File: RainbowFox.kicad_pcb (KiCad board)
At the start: 2 copper layers, 304.8 x 95.3 mm, 316 parts, among them P1 FLASH_HDR, P2 CONN_01X06, P3 USB_OTG, P4 CONN_01X04, P5 CONN_01X02, P6 CONN_01X04, U1 MK20DX256VLH7, U2 IS31FL3737, U3 IS31FL3737, X1 CRYSTAL_SMD

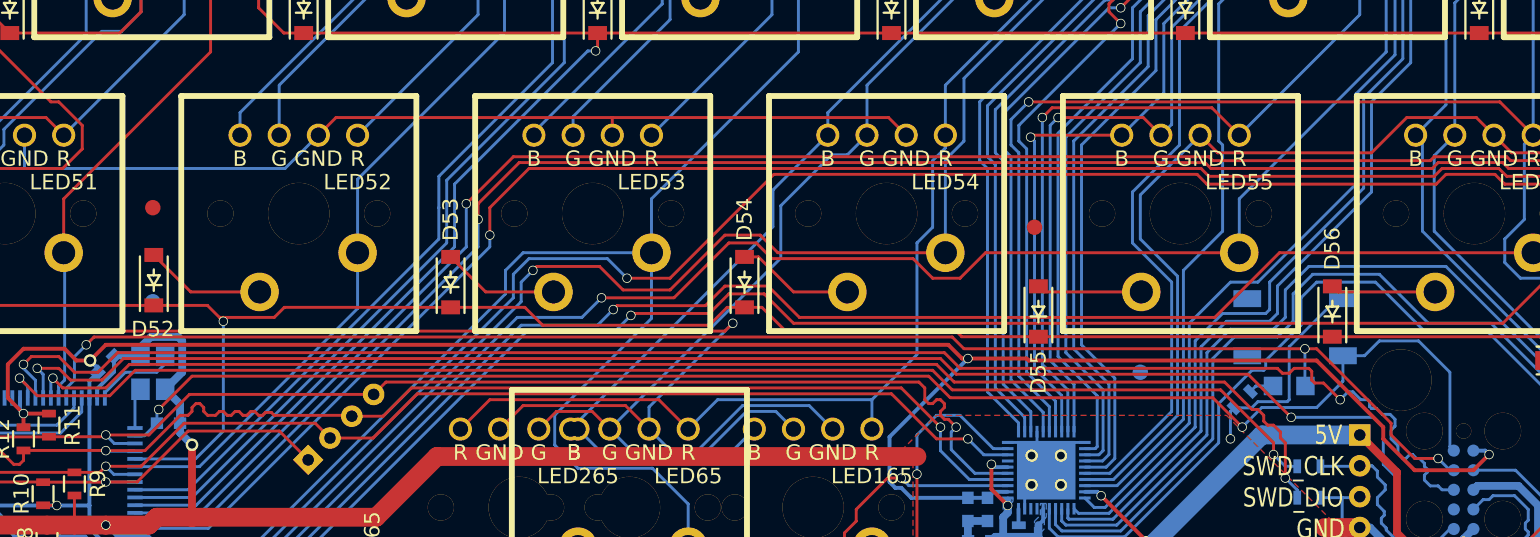
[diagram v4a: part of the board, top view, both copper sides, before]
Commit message: Properly replaced the Footprint of the Reset Switch
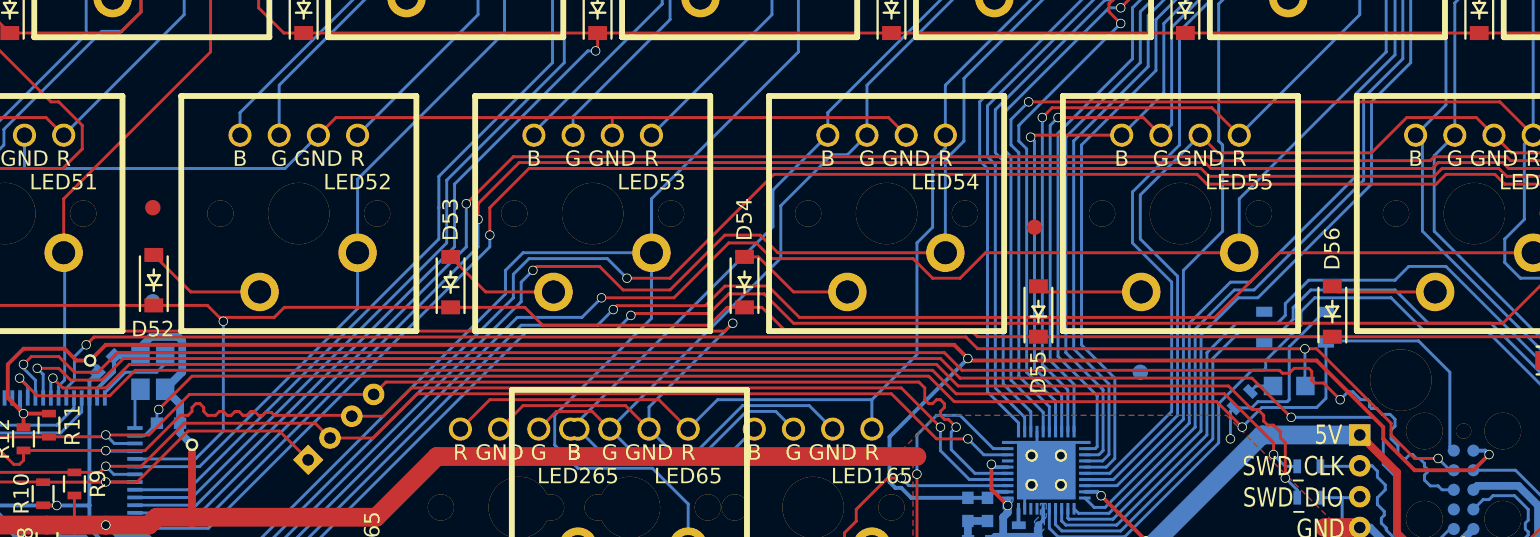
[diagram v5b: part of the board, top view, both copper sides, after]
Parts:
- S72: footprint lib.pretty:TACT_5.2x5.2 -> lib.pretty:PTS810
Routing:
- net GND: track 348.6 -> 346.4 mm
- net /ledmatrix/LED-B/CS9: track 176.0 -> 174.6 mm
- net /ledmatrix/LED-B/CS10: track 232.5 -> 231.2 mm
- net /mcu/MCU_RESET: track 98.0 -> 99.2 mm
- net /ledmatrix/LED-B/CS6: track 208.5 -> 207.6 mm
- net /ledmatrix/LED-B/CS7: track 241.7 -> 240.8 mm
- net /ledmatrix/LED-B/CS8: track 86.2 -> 85.6 mm
